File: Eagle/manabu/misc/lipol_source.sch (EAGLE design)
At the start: 29 parts, among them T1 FDV304P, U1 16F1454, U2 NC7SB3157P6X, U3 NC7SB3157P6X

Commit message: preparation for the seed studio PCB maker
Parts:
- removed TP1: TPB1,27, testpad:TPB1,27
- added FLASH: TPTP10R, testpad:TPTP10R
- C1, C2, C3, C5: value 100nF -> 100n
- C4, C6, C7: value 4.7uF -> 4.7u
- C8: value 470pF -> 470p
- TC1185: value STABILISER_APE8865 -> TC1185
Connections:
- net N$1: now also FLASH.TP; no longer TP1.TP
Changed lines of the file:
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@@
 <parts>
 <part name="U1" library="!stavebnice03" deviceset="16F1454" device=""/>
-<part name="C2" library="resistor" deviceset="C-EU" device="C0603K" value="100nF"/>
+<part name="C2" library="resistor" deviceset="C-EU" device="C0603K" value="100n"/>
 <part name="R1" library="resistor" deviceset="R-EU_" device="R0603" value="2k2"/>
 <part name="R2" library="resistor" deviceset="R-EU_" device="R0603" value="2k2"/>
-<part name="C3" library="resistor" deviceset="C-EU" device="C0603K" value="100nF"/>
+<part name="C3" library="resistor" deviceset="C-EU" device="C0603K" value="100n"/>
 <part name="OUT" library="!stavebnice03" deviceset="JUMPER5F-90" device=""/>
 <part name="U3" library="!stavebnice03" deviceset="NC7SB3157P6X" device=""/>
 <part name="U2" library="!stavebnice03" deviceset="NC7SB3157P6X" device=""/>
-<part name="C5" library="resistor" deviceset="C-EU" device="C0603K" value="100nF"/>
+<part name="C5" library="resistor" deviceset="C-EU" device="C0603K" value="100n"/>
 <part name="USB" library="!stavebnice03" deviceset="USBMICRO" device=""/>
-<part name="C1" library="resistor" deviceset="C-EU" device="C0603K" value="100nF"/>
+<part name="C1" library="resistor" deviceset="C-EU" device="C0603K" value="100n"/>
 <part name="U$3" library="!stavebnice03" deviceset="LIPOL_21X17" device=""/>
 <part name="MCP73832" library="!stavebnice03" deviceset="MCP73831" device=""/>
 <part name="R3" library="resistor" deviceset="R-EU_" device="R0603" value="22k"/>
-<part name="C4" library="resistor" deviceset="C-EU" device="C0603K" value="4.7uF"/>
-<part name="C6" library="resistor" deviceset="C-EU" device="C0603K" value="4.7uF"/>
-<part name="TC1185" library="!stavebnice03" deviceset="STABILISER_APE8865" device=""/>
+<part name="C4" library="resistor" deviceset="C-EU" device="C0603K" value="4.7u"/>
+<part name="C6" library="resistor" deviceset="C-EU" device="C0603K" value="4.7u"/>
+<part name="TC1185" library="!stavebnice03" deviceset="STABILISER_APE8865" device="" value="TC1185"/>
 <part name="T1" library="!stavebnice03" deviceset="P-MOSFET-FDV304P" device="" value="FDV304P"/>
 <part name="R4" library="resistor" deviceset="R-EU_" device="R0603" value="100k"/>
-<part name="C7" library="resistor" deviceset="C-EU" device="C0603K" value="4.7uF"/>
+<part name="C7" library="resistor" deviceset="C-EU" device="C0603K" value="4.7u"/>
 <part name="PROG" library="!stavebnice03" deviceset="JUMPER5M" device=""/>
 <part name="R5" library="resistor" deviceset="R-EU_" device="R0603" value="100k"/>
 <part name="R6" library="resistor" deviceset="R-EU_" device="R0603" value="2k2"/>
-<part name="C8" library="resistor" deviceset="C-EU" device="C0603K" value="470pF"/>
+<part name="C8" library="resistor" deviceset="C-EU" device="C0603K" value="470p"/>
 <part name="R7" library="resistor" deviceset="R-EU_" device="R0603" value="100k"/>
 <part name="RESET" library="!stavebnice03" deviceset="BYTTON-B3U" device=""/>
 <part name="D1" library="!stavebnice03" deviceset="LED1.8" device=""/>
 <part name="R8" library="resistor" deviceset="R-EU_" device="R0603" value="100k"/>
-<part name="TP1" library="testpad" deviceset="TP" device="B1,27"/>
+<part name="FLASH" library="testpad" deviceset="TP" device="TP10R" value="TPTP10R"/>
 </parts>
 <sheets>
@@
 <instance part="D1" gate="G$1" x="86.36" y="66.04" rot="R90"/>
 <instance part="R8" gate="G$1" x="114.3" y="101.6" rot="R270"/>
-<instance part="TP1" gate="G$1" x="106.68" y="96.52"/>
+<instance part="FLASH" gate="G$1" x="106.68" y="96.52"/>
 </instances>
 <busses>
@@
 <wire x1="114.3" y1="93.98" x2="114.3" y2="96.52" width="0.1524" layer="91"/>
 <junction x="114.3" y="93.98"/>
-<pinref part="TP1" gate="G$1" pin="TP"/>
+<pinref part="FLASH" gate="G$1" pin="TP"/>
 <wire x1="106.68" y1="93.98" x2="114.3" y2="93.98" width="0.1524" layer="91"/>
 </segment>

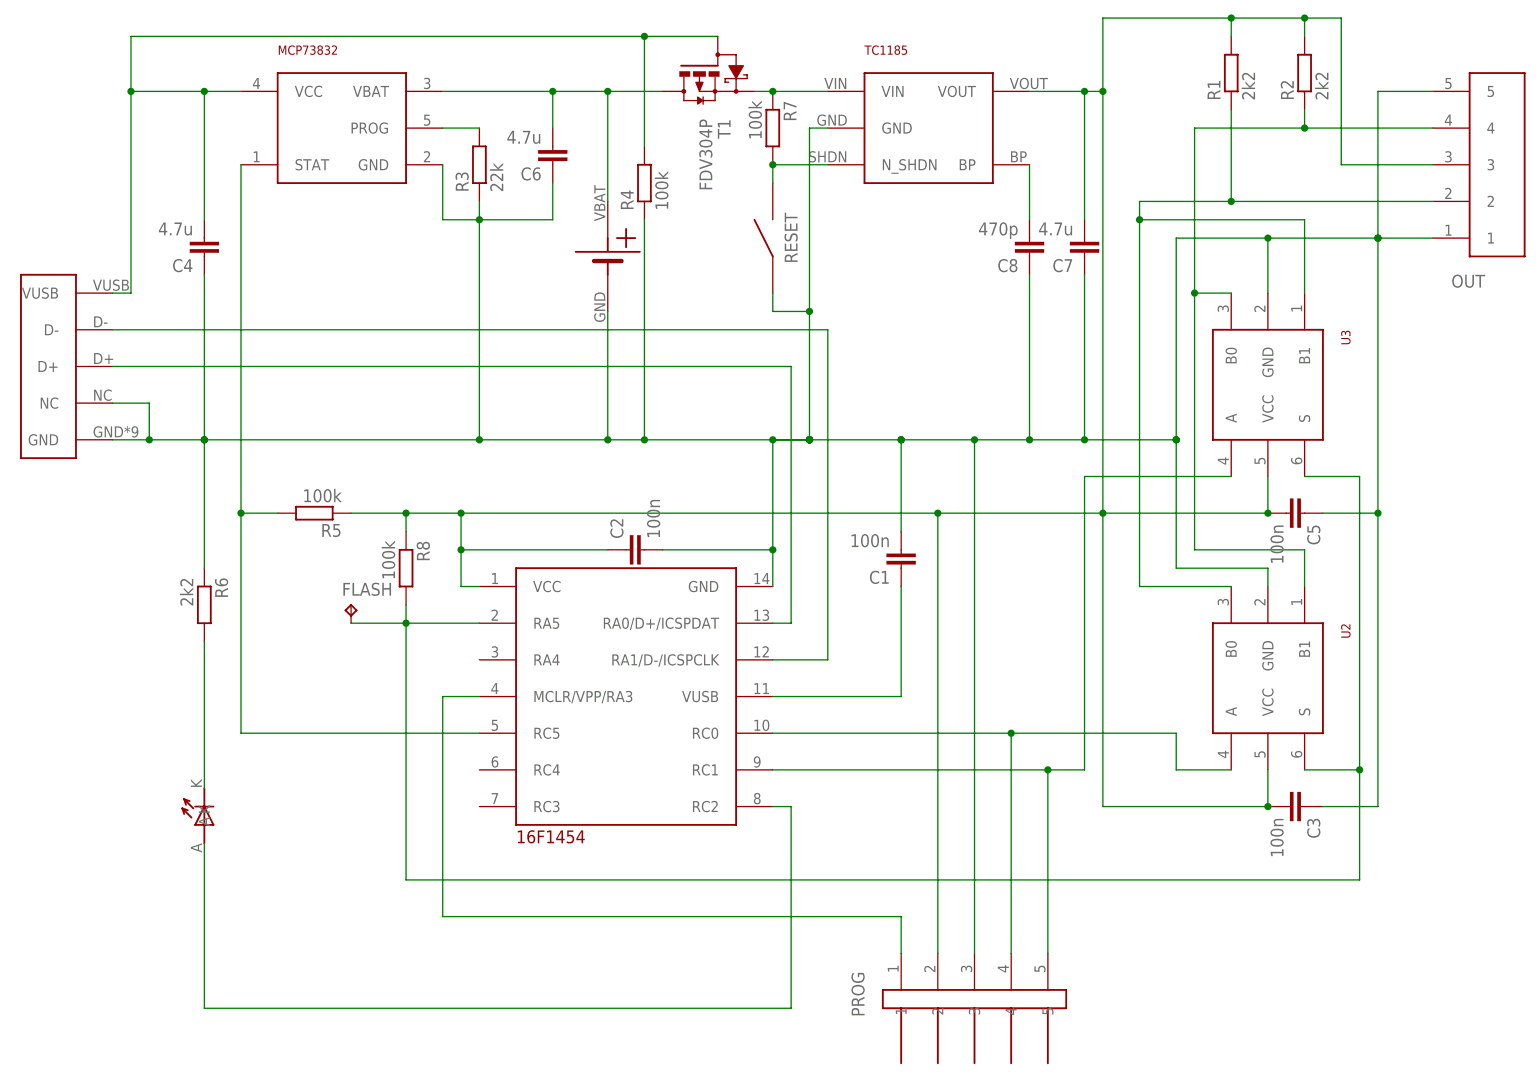
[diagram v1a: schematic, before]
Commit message: invert output functionality moved to lipol module port A4 to be as same as on other modules (bootloader reset pin will have to be changed for lipol module)
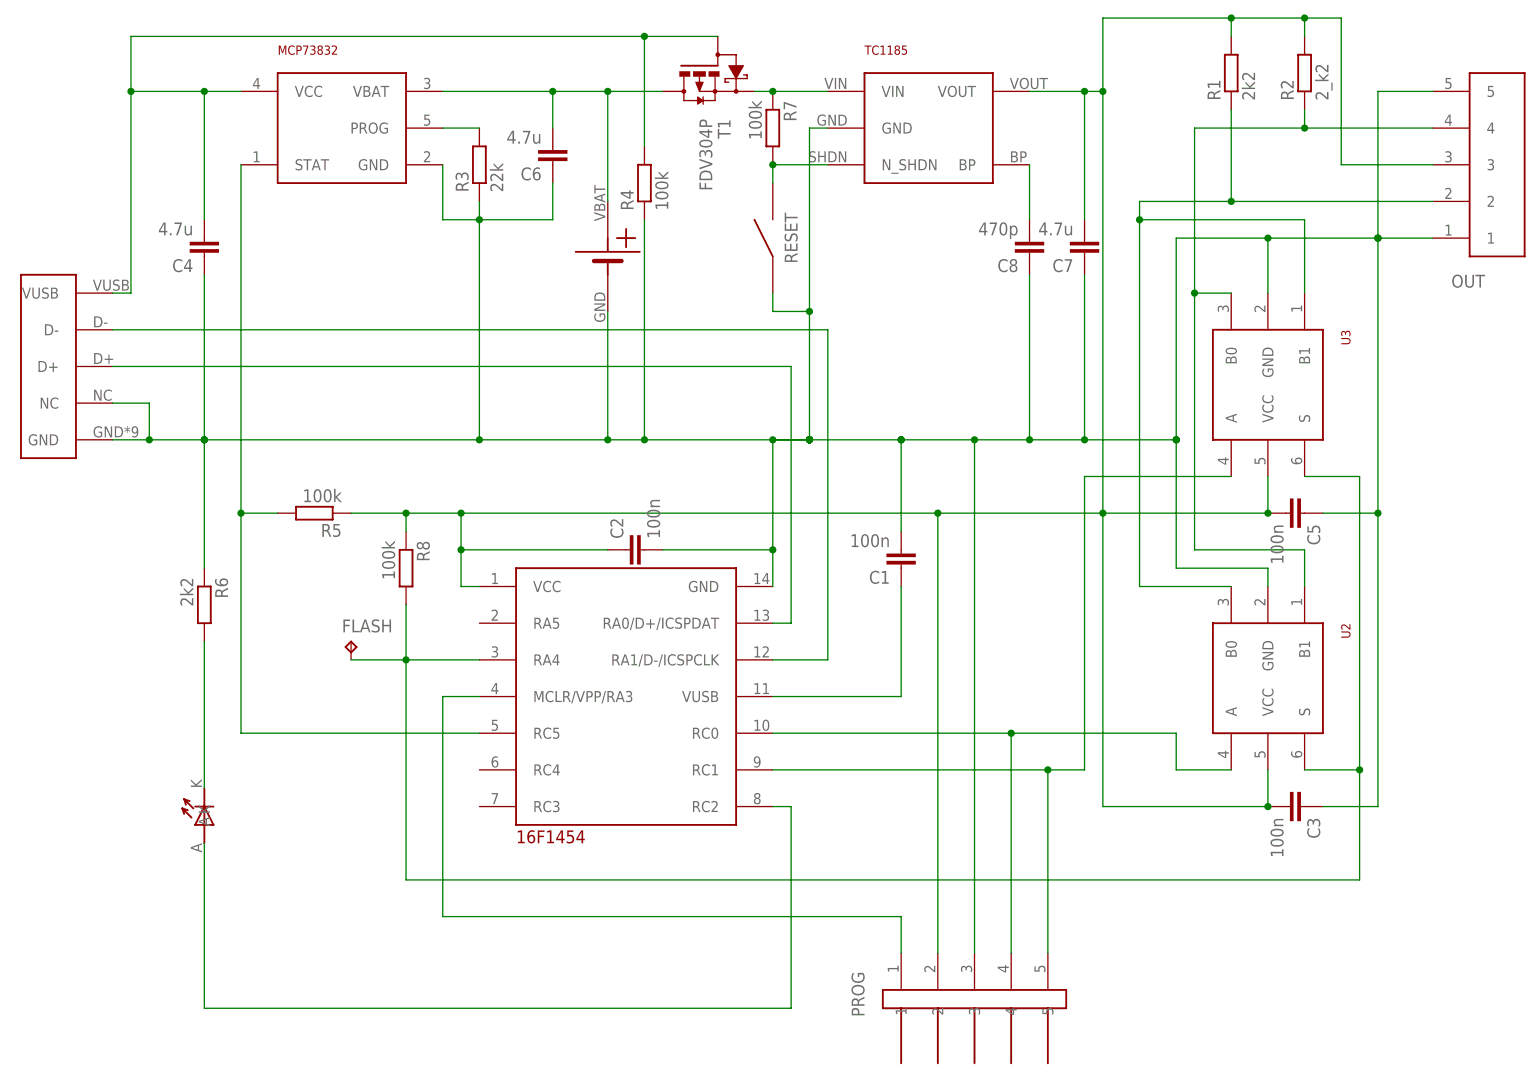
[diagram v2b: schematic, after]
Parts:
- R2: value 2k2 -> 2_k2
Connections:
- net N$1: now also U1.RA4; no longer U1.RA5
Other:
- moved on the sheet: FLASH
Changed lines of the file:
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@@
 <?xml version="1.0" encoding="utf-8"?>
 <!DOCTYPE eagle SYSTEM "eagle.dtd">
-<eagle version="7.2.0">
+<eagle version="7.4.0">
 <drawing>
 <settings>
@@
 <part name="C2" library="resistor" deviceset="C-EU" device="C0603K" value="100n"/>
 <part name="R1" library="resistor" deviceset="R-EU_" device="R0603" value="2k2"/>
-<part name="R2" library="resistor" deviceset="R-EU_" device="R0603" value="2k2"/>
+<part name="R2" library="resistor" deviceset="R-EU_" device="R0603" value="2_k2"/>
 <part name="C3" library="resistor" deviceset="C-EU" device="C0603K" value="100n"/>
 <part name="OUT" library="!stavebnice03" deviceset="JUMPER5F-90" device=""/>
@@
 <instance part="D1" gate="G$1" x="86.36" y="66.04" rot="R90"/>
 <instance part="R8" gate="G$1" x="114.3" y="101.6" rot="R270"/>
-<instance part="FLASH" gate="G$1" x="106.68" y="96.52"/>
+<instance part="FLASH" gate="G$1" x="106.68" y="91.44"/>
 </instances>
 <busses>
@@
 <wire x1="246.38" y1="73.66" x2="246.38" y2="58.42" width="0.1524" layer="91"/>
 <wire x1="246.38" y1="58.42" x2="114.3" y2="58.42" width="0.1524" layer="91"/>
-<wire x1="114.3" y1="58.42" x2="114.3" y2="93.98" width="0.1524" layer="91"/>
+<wire x1="114.3" y1="58.42" x2="114.3" y2="88.9" width="0.1524" layer="91"/>
 <pinref part="U2" gate="G$1" pin="S"/>
 <wire x1="238.76" y1="73.66" x2="246.38" y2="73.66" width="0.1524" layer="91"/>
@@
 <wire x1="246.38" y1="114.3" x2="238.76" y2="114.3" width="0.1524" layer="91"/>
 <junction x="246.38" y="73.66"/>
-<pinref part="U1" gate="G$1" pin="RA5"/>
-<wire x1="114.3" y1="93.98" x2="124.46" y2="93.98" width="0.1524" layer="91"/>
 <pinref part="R8" gate="G$1" pin="2"/>
-<wire x1="114.3" y1="93.98" x2="114.3" y2="96.52" width="0.1524" layer="91"/>
-<junction x="114.3" y="93.98"/>
+<wire x1="114.3" y1="88.9" x2="114.3" y2="96.52" width="0.1524" layer="91"/>
+<junction x="114.3" y="88.9"/>
 <pinref part="FLASH" gate="G$1" pin="TP"/>
-<wire x1="106.68" y1="93.98" x2="114.3" y2="93.98" width="0.1524" layer="91"/>
-</segment>
-</net>
+<wire x1="106.68" y1="88.9" x2="114.3" y2="88.9" width="0.1524" layer="91"/>
+<pinref part="U1" gate="G$1" pin="RA4"/>
+<wire x1="124.46" y1="88.9" x2="114.3" y2="88.9" width="0.1524" layer="91"/>
+</segment>
+</net>
